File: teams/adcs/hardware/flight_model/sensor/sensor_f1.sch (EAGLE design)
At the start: 73 parts, among them U1 LT1761-X, U2 LT1761-X, U3 OEM719, U4 LTC3624

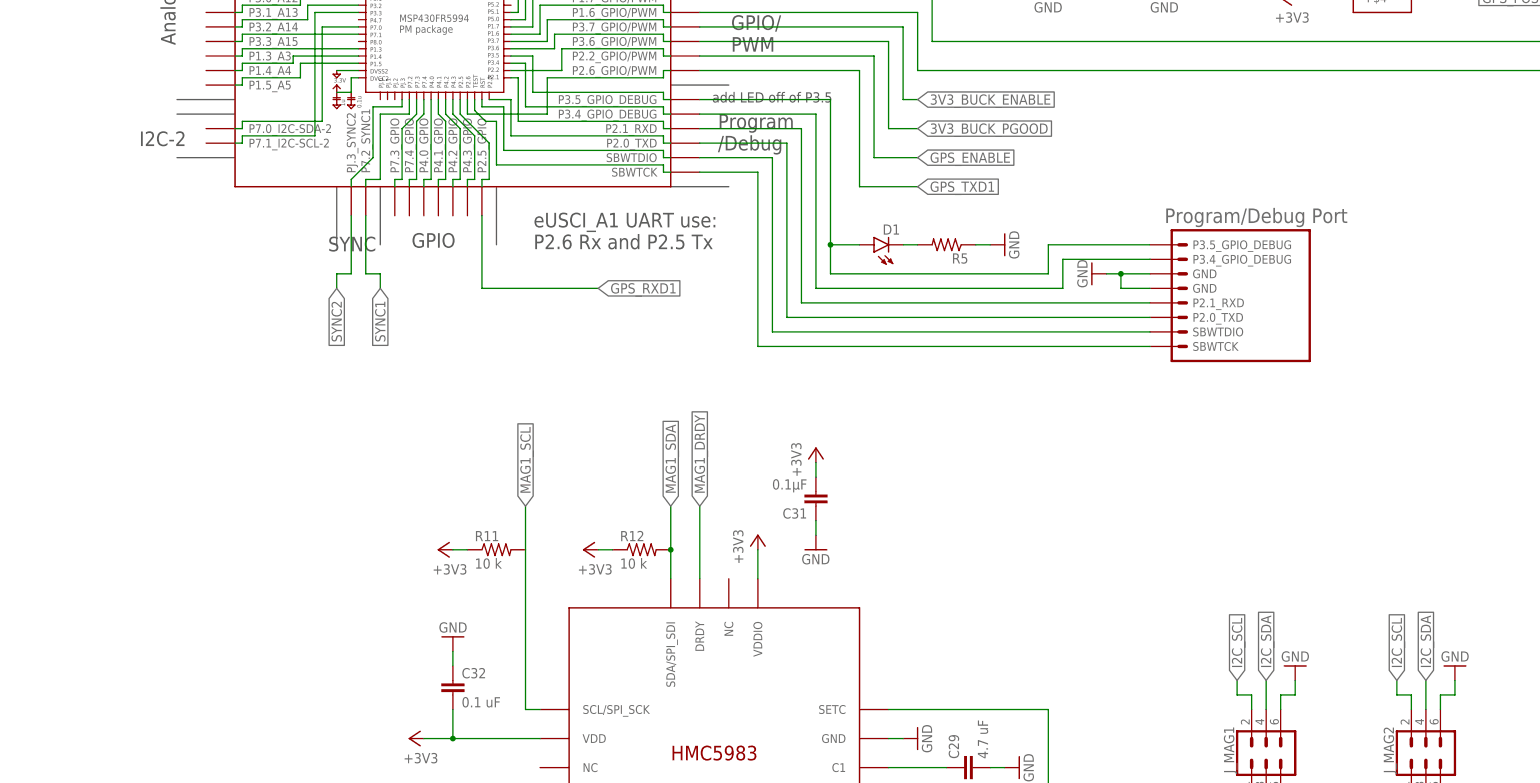
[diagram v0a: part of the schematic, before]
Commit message: ADCS/Sensor: Rename board files and reconnect second magnetometer ti I2C bus 2
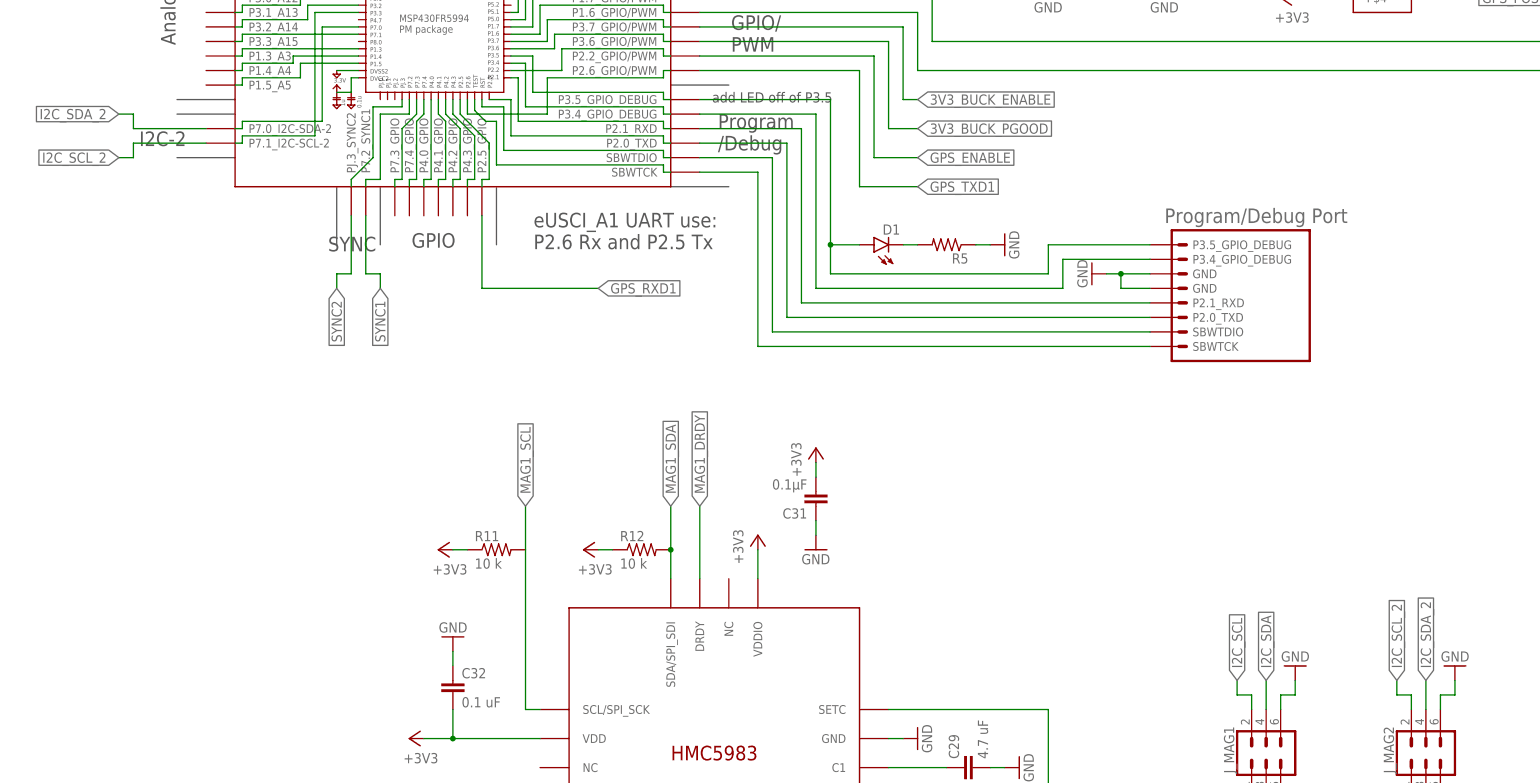
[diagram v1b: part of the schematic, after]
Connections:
- new net I2C_SCL_2: BLK1.P7.1_I2C-SCL-2, J_MAG2.2
- new net I2C_SDA_2: BLK1.P7.0_I2C-SDA-2, J_MAG2.4
- net I2C_SCL: no longer J_MAG2.2
- net I2C_SDA: no longer J_MAG2.4
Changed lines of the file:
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@@
-</segment>
-<segment>
-<pinref part="J_MAG2" gate="G$1" pin="4"/>
-<wire x1="203.2" y1="-208.28" x2="203.2" y2="-203.2" width="0.1524" layer="91"/>
-<label x="203.2" y="-203.2" size="1.778" layer="95" rot="R90" xref="yes"/>
 </segment>
 <segment>
@@
 <wire x1="170.18" y1="-205.74" x2="170.18" y2="-203.2" width="0.1524" layer="91"/>
 <label x="170.18" y="-203.2" size="1.778" layer="95" rot="R90" xref="yes"/>
-</segment>
-<segment>
-<pinref part="J_MAG2" gate="G$1" pin="2"/>
-<wire x1="200.66" y1="-208.28" x2="200.66" y2="-205.74" width="0.1524" layer="91"/>
-<wire x1="200.66" y1="-205.74" x2="198.12" y2="-205.74" width="0.1524" layer="91"/>
-<wire x1="198.12" y1="-205.74" x2="198.12" y2="-203.2" width="0.1524" layer="91"/>
-<label x="198.12" y="-203.2" size="1.778" layer="95" rot="R90" xref="yes"/>
 </segment>
 <segment>
@@
 </segment>
 </net>
+<net name="I2C_SCL_2" class="0">
+<segment>
+<pinref part="J_MAG2" gate="G$1" pin="2"/>
+<wire x1="200.66" y1="-208.28" x2="200.66" y2="-205.74" width="0.1524" layer="91"/>
+<wire x1="200.66" y1="-205.74" x2="198.12" y2="-205.74" width="0.1524" layer="91"/>
+<wire x1="198.12" y1="-205.74" x2="198.12" y2="-203.2" width="0.1524" layer="91"/>
+<label x="198.12" y="-203.2" size="1.778" layer="95" rot="R90" xref="yes"/>
+</segment>
+<segment>
+<pinref part="BLK1" gate="G$1" pin="P7.1_I2C-SCL-2"/>
+<wire x1="-10.16" y1="-109.22" x2="-22.86" y2="-109.22" width="0.1524" layer="91"/>
+<wire x1="-22.86" y1="-109.22" x2="-22.86" y2="-111.76" width="0.1524" layer="91"/>
+<wire x1="-22.86" y1="-111.76" x2="-25.4" y2="-111.76" width="0.1524" layer="91"/>
+<label x="-25.4" y="-111.76" size="1.778" layer="95" rot="R180" xref="yes"/>
+</segment>
+</net>
+<net name="I2C_SDA_2" class="0">
+<segment>
+<pinref part="J_MAG2" gate="G$1" pin="4"/>
+<wire x1="203.2" y1="-208.28" x2="203.2" y2="-203.2" width="0.1524" layer="91"/>
+<label x="203.2" y="-203.2" size="1.778" layer="95" rot="R90" xref="yes"/>
+</segment>
+<segment>
+<pinref part="BLK1" gate="G$1" pin="P7.0_I2C-SDA-2"/>
+<wire x1="-10.16" y1="-106.68" x2="-22.86" y2="-106.68" width="0.1524" layer="91"/>
+<wire x1="-22.86" y1="-106.68" x2="-22.86" y2="-104.14" width="0.1524" layer="91"/>
+<wire x1="-22.86" y1="-104.14" x2="-25.4" y2="-104.14" width="0.1524" layer="91"/>
+<label x="-25.4" y="-104.14" size="1.778" layer="95" rot="R180" xref="yes"/>
+</segment>
+</net>

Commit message: Flight merge (#230)
Merge of the flight code into master
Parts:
- R1, R2: value 2.2k -> DNP
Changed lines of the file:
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@@
 <?xml version="1.0" encoding="utf-8"?>
 <!DOCTYPE eagle SYSTEM "eagle.dtd">
-<eagle version="8.7.1">
+<eagle version="8.4.2">
 <drawing>
 <settings>
@@
 <part name="+3V34" library="supply1" library_urn="urn:adsk.eagle:library:371" deviceset="+3V3" device=""/>
 <part name="+3V35" library="supply1" library_urn="urn:adsk.eagle:library:371" deviceset="+3V3" device=""/>
-<part name="R1" library="DubSat1 Components" deviceset="RESISTOR" device="0805" value="2.2k"/>
-<part name="R2" library="DubSat1 Components" deviceset="RESISTOR" device="0805" value="2.2k"/>
+<part name="R1" library="DubSat1 Components" deviceset="RESISTOR" device="0805" value="DNP"/>
+<part name="R2" library="DubSat1 Components" deviceset="RESISTOR" device="0805" value="DNP"/>
 <part name="+3V32" library="supply1" library_urn="urn:adsk.eagle:library:371" deviceset="+3V3" device=""/>
 <part name="+3V33" library="supply1" library_urn="urn:adsk.eagle:library:371" deviceset="+3V3" device=""/>
